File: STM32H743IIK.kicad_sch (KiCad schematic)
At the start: 35 parts, among them U1 STM32H743IIKx, Y1 25MHz, Y2 32.768KHz

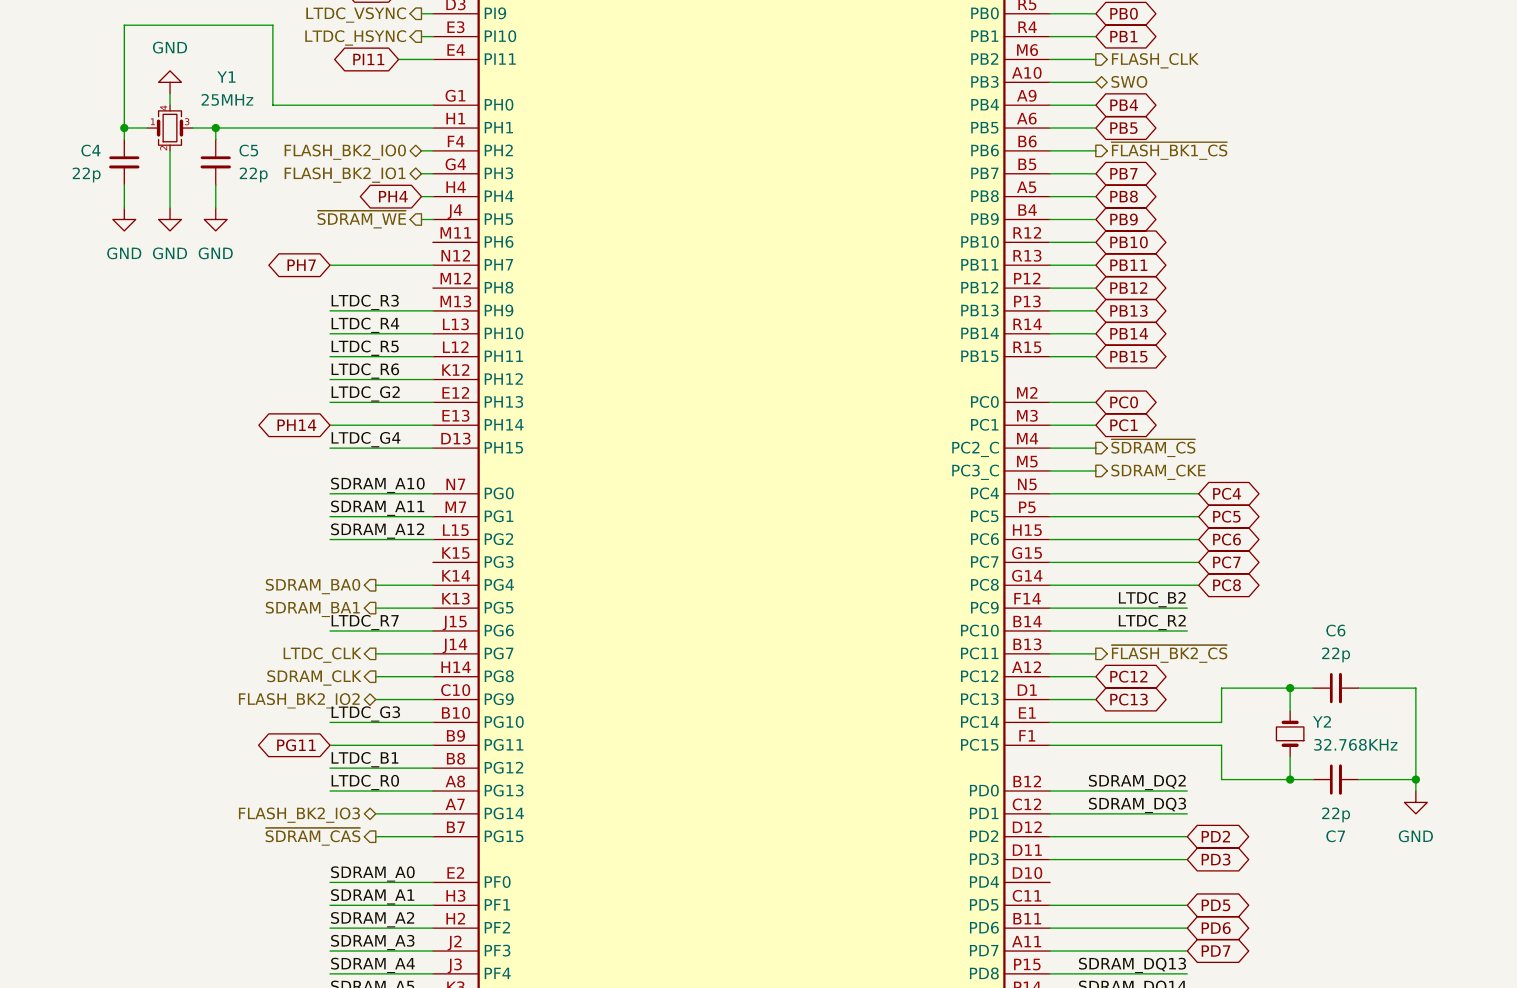
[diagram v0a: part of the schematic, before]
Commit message: Adding JLCPCB Part #
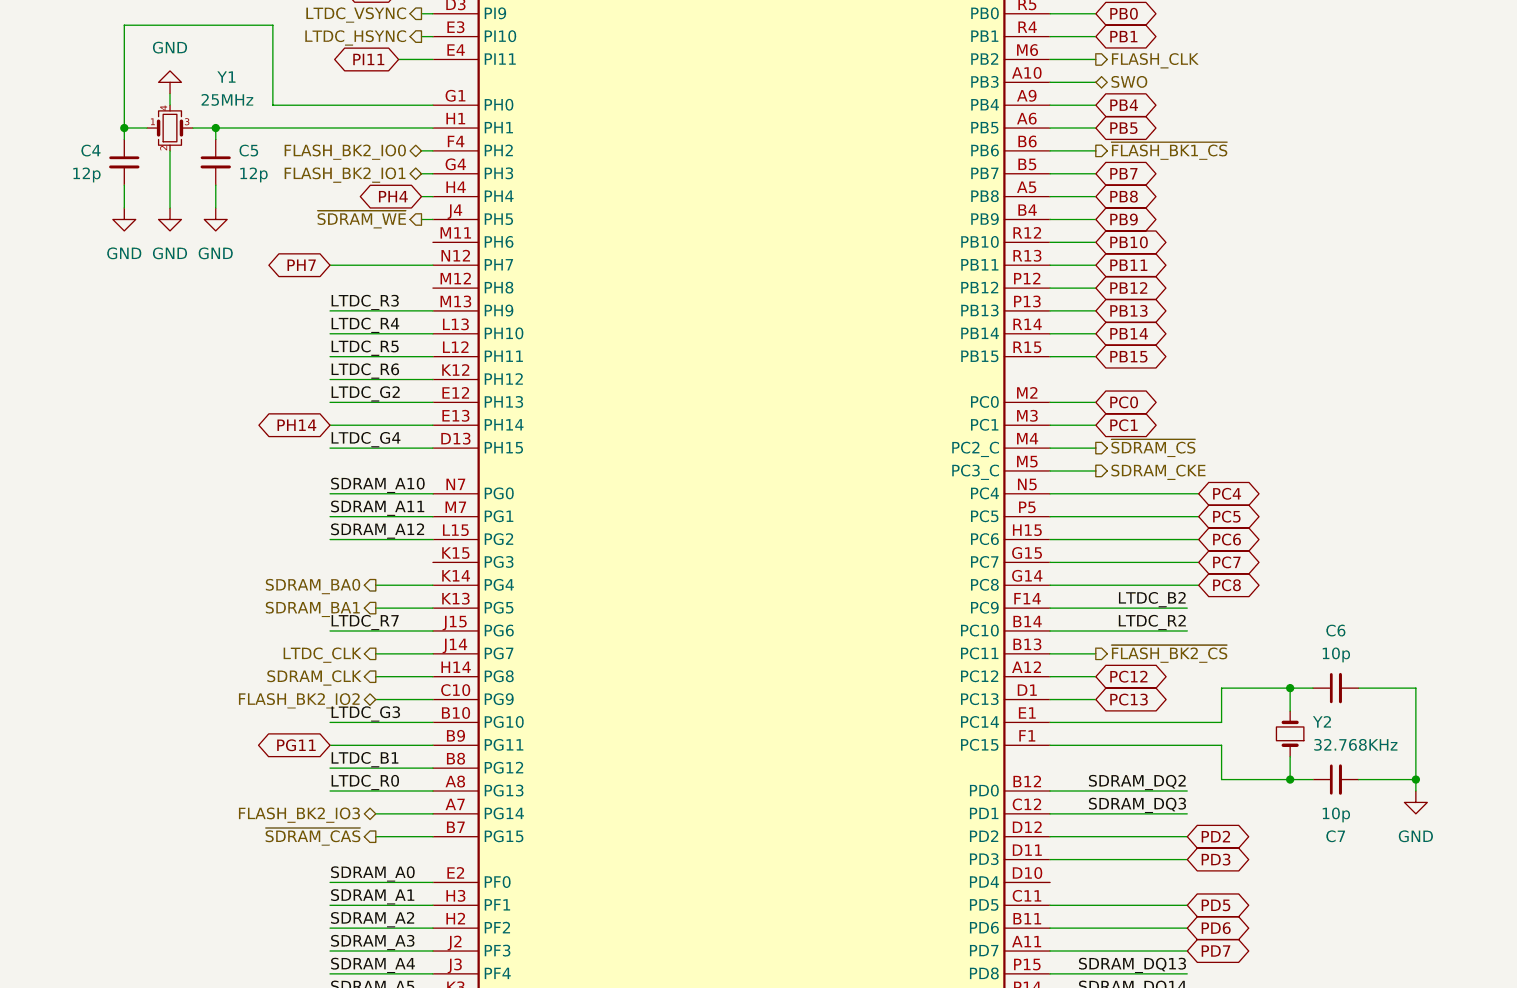
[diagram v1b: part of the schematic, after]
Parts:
- C1, C2: JLCPCB Part # (none) -> C12530
- C10: footprint Capacitor_SMD:C_0402_1005Metric -> Capacitor_SMD:C_0603_1608Metric; JLCPCB Part # (none) -> C96446
- C11, C12, C13, C14, C15, C16, C17, C18, C19, C20, C21, C22, C23, C24, C25, C3, C39, C9: JLCPCB Part # (none) -> C307380
- C4, C5: value 22p -> 12p; JLCPCB Part # (none) -> C277478
- C40, C8: JLCPCB Part # (none) -> C52923
- C6, C7: value 22p -> 10p; JLCPCB Part # (none) -> C76921
- D1: JLCPCB Part # (none) -> C37704
- L1: JLCPCB Part # (none) -> C76891
- R1, R2, R3: JLCPCB Part # (none) -> C473048
- U1: JLCPCB Part # (none) -> C129442
- Y1: JLCPCB Part # (none) -> C193187
- Y2: JLCPCB Part # (none) -> C99009

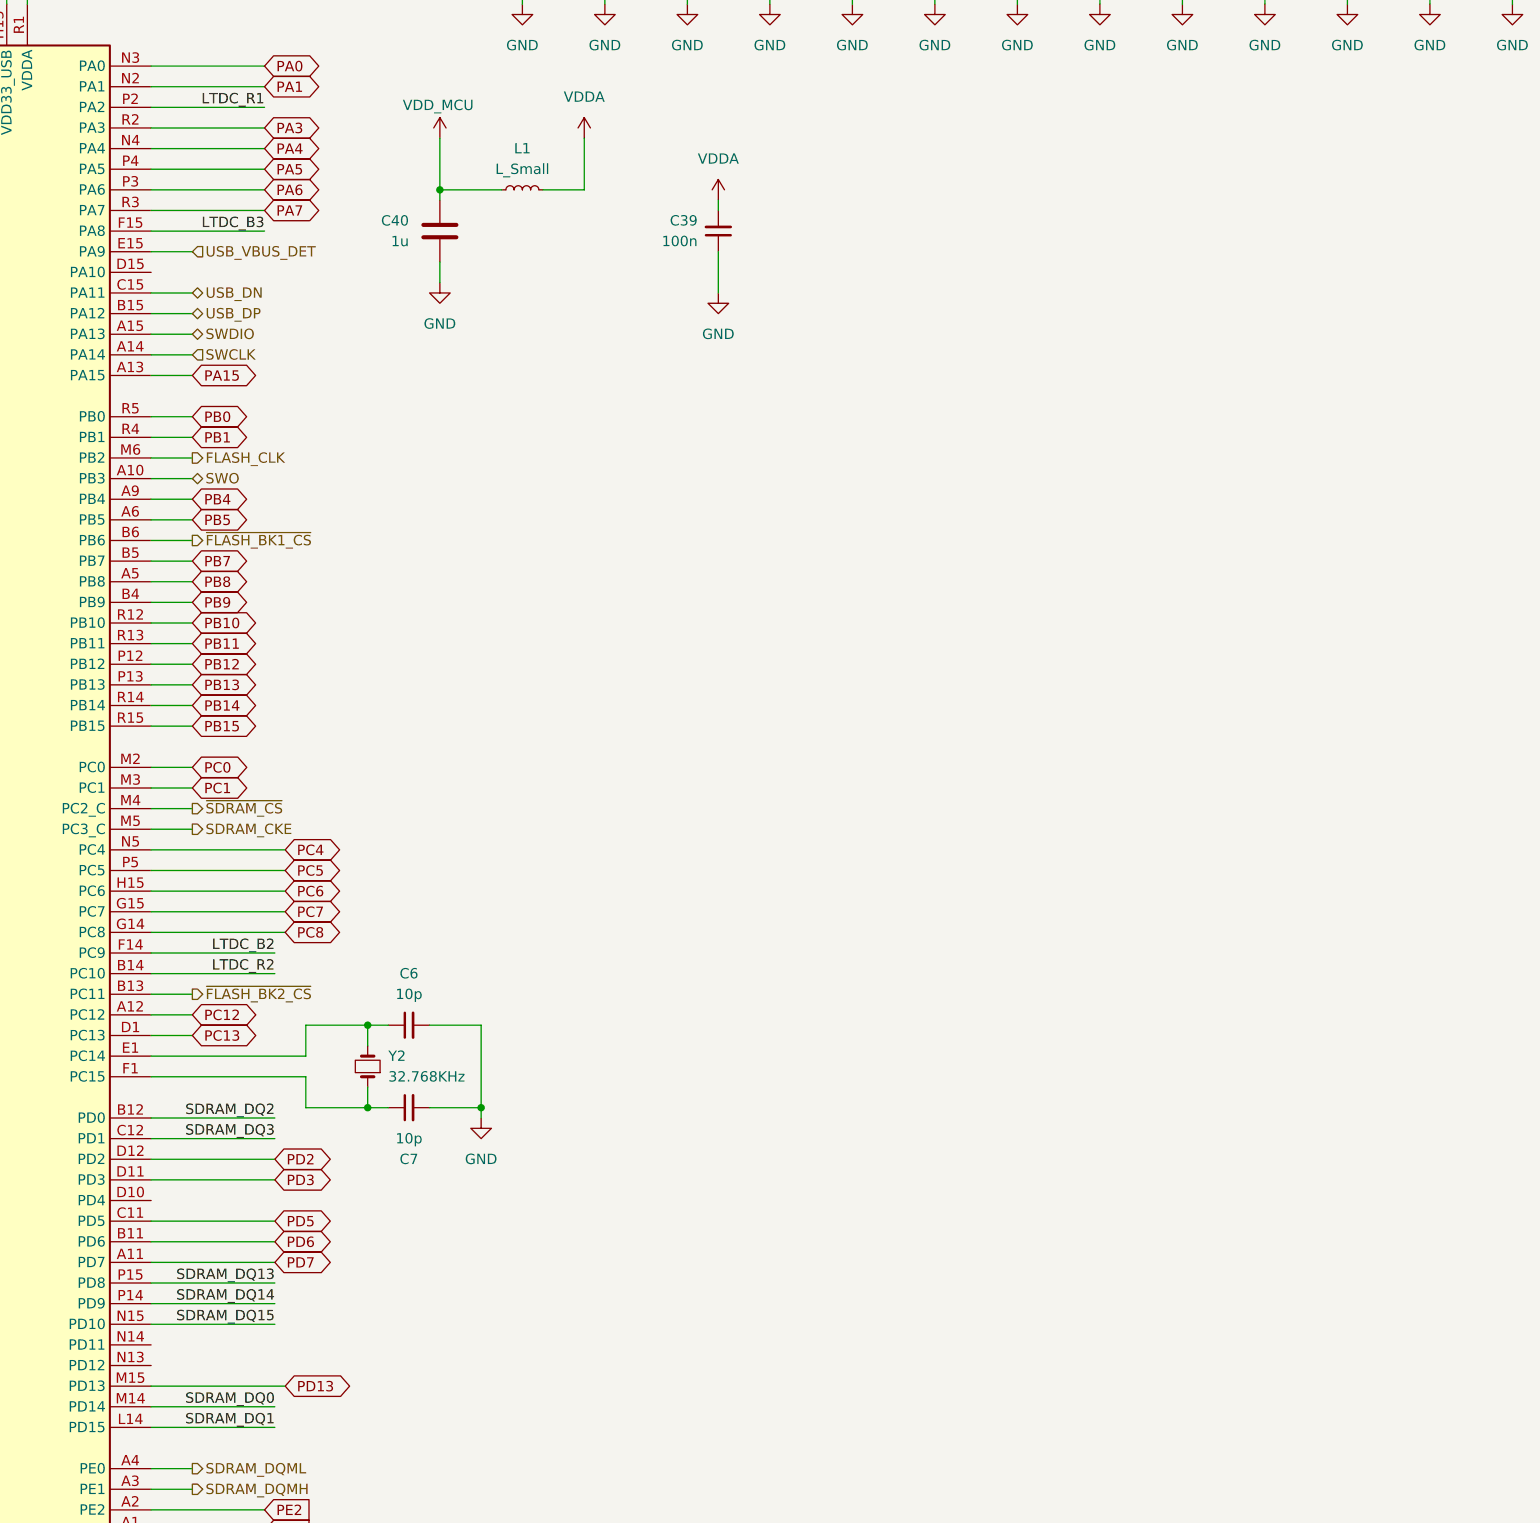
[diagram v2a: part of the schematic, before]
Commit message: SDRAM finished, changed castellated to 23pin each side, few pins unconnected
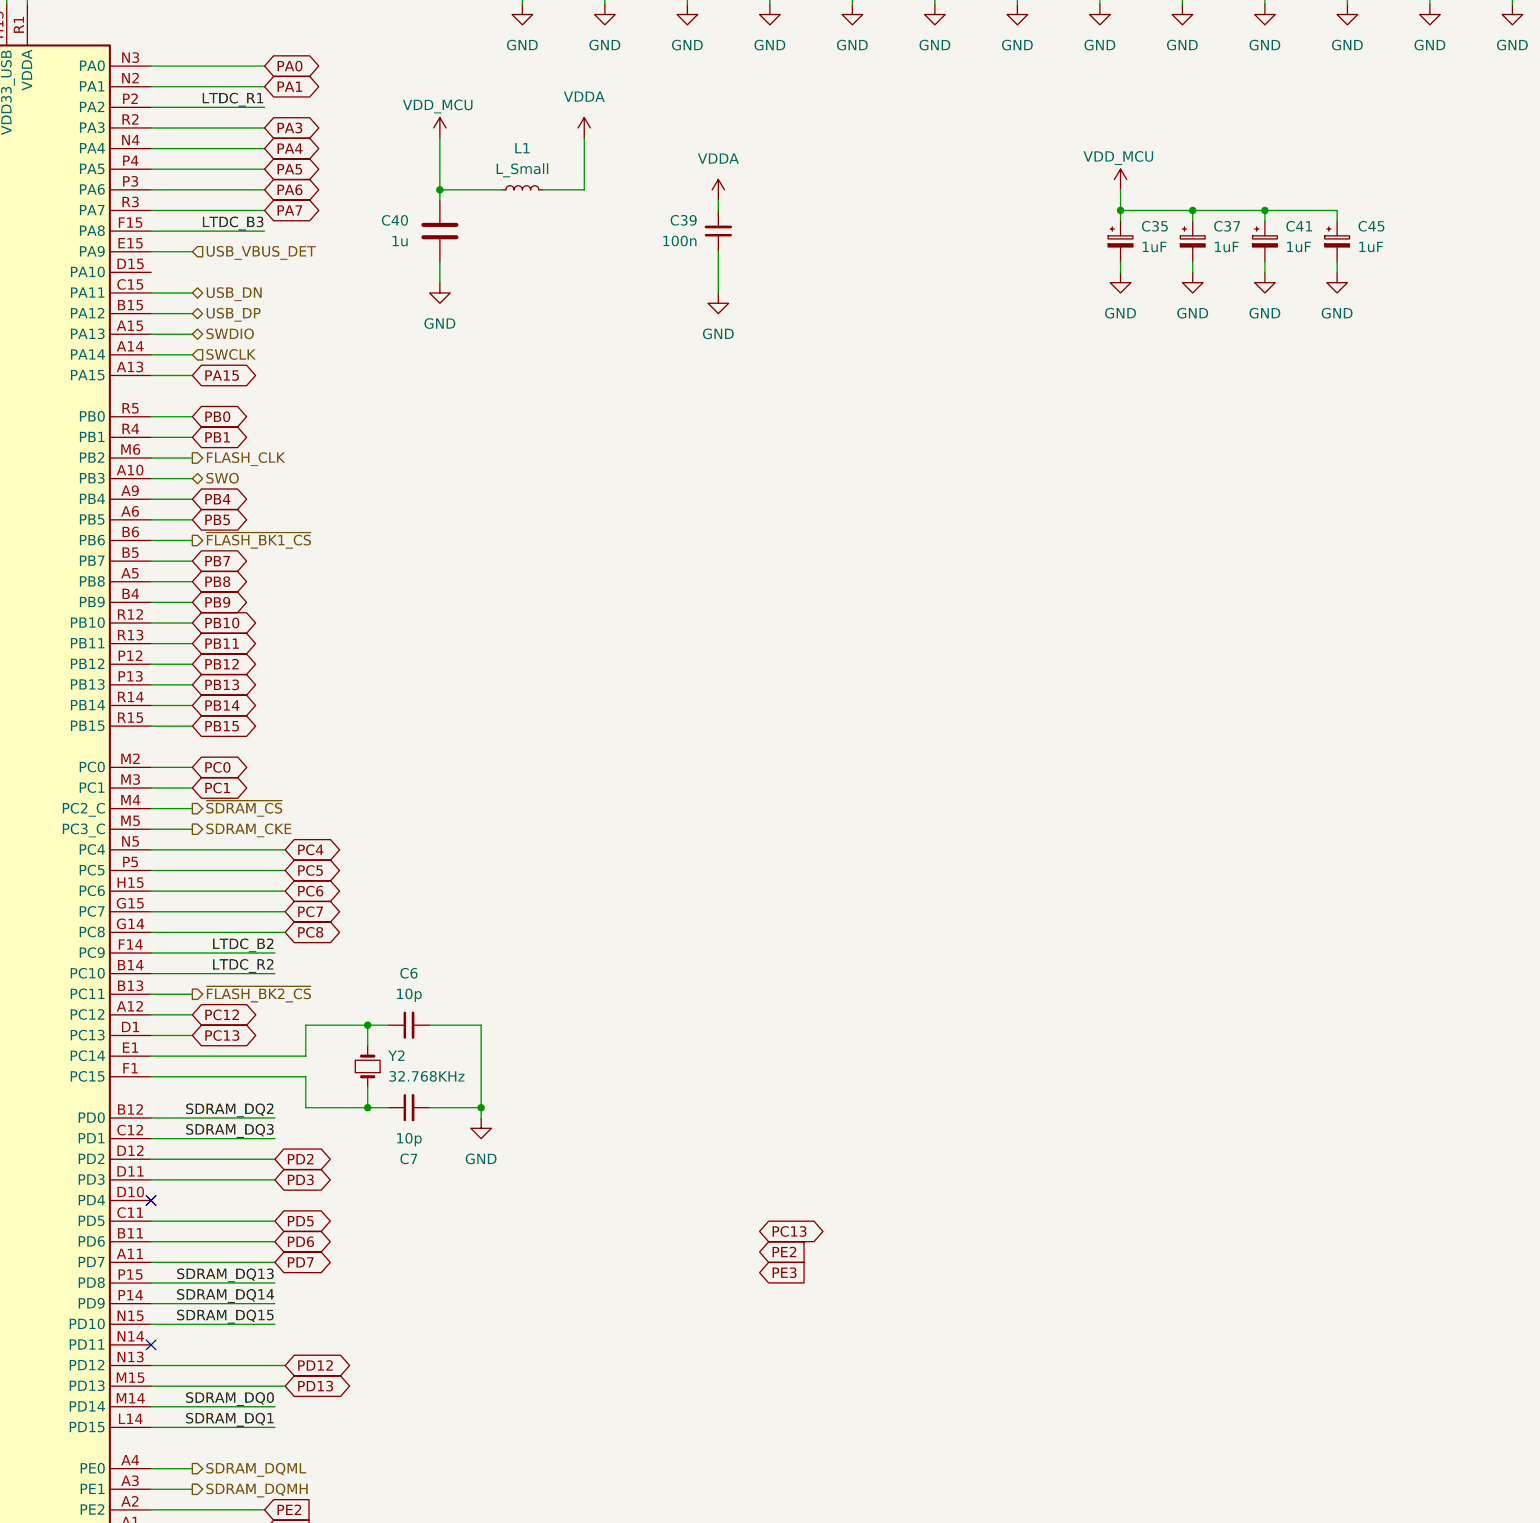
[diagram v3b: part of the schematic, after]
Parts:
- added C35, C37, C41, C45: 1uF, Capacitor_Tantalum_SMD:CP_EIA-1608-08_AVX-J, symbol Device:C_Polarized_Small
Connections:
- net +3V3: now also C35.1, C37.1, C41.1, C45.1
- net GND: now also C35.2, C37.2, C41.2, C45.2
- net PD12: now reaches U1.N13 (PD12)
- no-connect marks 0 -> 2
